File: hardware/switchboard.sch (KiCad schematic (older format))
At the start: 0 parts

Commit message: hardware: add terminal blocks
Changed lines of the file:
@@
 $Descr A4 11693 8268
 encoding utf-8
-Sheet 1 3
+Sheet 1 4
 Title ""
 Date ""
@@
 $EndDescr
 $Sheet
-S 3085 2165 1515 1345
+S 3085 2165 1625 3010
 U 605C1303
 F0 "Relays" 50
 F1 "relays.sch" 50
+F2 "DOME_LIGHTS" I R 4710 2320 50
+F3 "WATER_PUMP" I R 4710 2450 50
+F4 "FRIDGE" I R 4710 2575 50
+F5 "STRIP_LIGHTS" I R 4710 2695 50
+F6 "REAR_FLOOD" I R 4710 2815 50
+F7 "DRIVER_FLOOD" I R 4710 2900 50
+F8 "PASS_FLOOD" I R 4710 3035 50
+F9 "DIESEL_HEATER" I R 4710 3160 50
+F10 "DOME_LIGHTS_CTRL" I L 3085 2535 50
+F11 "WATER_PUMP_CTRL" I L 3085 2355 50
+F12 "FRIDGE_CTRL" I L 3085 2630 50
+F13 "STRIP_LIGHTS_CTRL" I L 3085 2750 50
+F14 "DIESEL_HEATER_CTRL" I L 3085 2905 50
+F15 "PASS_FLOOD_CTRL" I L 3085 3075 50
+F16 "DRIVER_FLOOD_CTRL" I L 3085 3245 50
+F17 "REAR_FLOOD_CTRL" I L 3085 3400 50
+F18 "SHOWER_FAN" I R 4710 3350 50
+F19 "SHOWER_FAN_CTRL" I L 3085 3555 50
+F20 "KITCHEN_FAN" I R 4710 3530 50
+F21 "KITCHEN_FAN_CTRL" I L 3085 3720 50
+F22 "BAR_LIGHT" I R 4710 3700 50
+F23 "BAR_LIGHT_CTRL" I L 3085 3890 50
+F24 "COMP_1_LIGHT_CTRL" I L 3085 4045 50
+F25 "COMP_1_LIGHT" I R 4710 3840 50
+F26 "COMP_4_LIGHT" I R 4710 3975 50
+F27 "COMP_4_LIGHT_CTRL" I L 3085 4190 50
+F28 "COMP_3_LIGHT" I R 4710 4110 50
+F29 "COMP_3_LIGHT_CTRL" I L 3085 4310 50
+F30 "COMP_2_LIGHT" I R 4710 4270 50
+F31 "COMP_2_LIGHT_CTRL" I L 3085 4410 50
+F32 "COMP_5_LIGHT_CTRL" I L 3085 4510 50
+F33 "COMP_5_LIGHT" I R 4710 4385 50
+F34 "AUX_RLY_1" I R 4710 4500 50
+F35 "AUX_RLY_1_CTRL" I L 3085 4695 50
+F36 "AUX_RLY_2" I R 4710 4635 50
+F37 "AUX_RLY_2_CTRL" I L 3085 4800 50
+F38 "AUX_RLY_3" I R 4710 4765 50
+F39 "AUX_RLY_3_CTRL" I L 3085 4905 50
+F40 "AUX_RLY_4" I R 4710 4880 50
+F41 "AUX_RLY_4_CTRL" I L 3085 5000 50
 $EndSheet
 $Sheet
@@
 F0 "Connectors" 50
 F1 "connectors.sch" 50
-F2 "P1[1..12]" I L 5825 2105 50
-F3 "P2[1..12]" I L 5825 2220 50
-F4 "P3[1..12]" I L 5825 2340 50
-F5 "P4[1..12]" I L 5825 2455 50
-F6 "P5[1..12]" I L 5825 2570 50
-F7 "P6[1..12]" I L 5825 2690 50
-F8 "P7[1..12]" I L 5825 2820 50
-F9 "P8[1..12]" I L 5825 2950 50
-F10 "P9[1..12]" I L 5825 3070 50
-F11 "P10[1..12]" I L 5825 3190 50
-F12 "P11[1..12]" I L 5825 3310 50
-F13 "P12[1..12]" I L 5825 3430 50
-F14 "AUX_SW_1" I R 7000 2180 50
-F15 "AUX_SW_2" I R 7000 2310 50
-F16 "AUX_SW_3" I R 7000 2425 50
-F17 "AUX_SW_4" I R 7000 2535 50
+$EndSheet
+$Sheet
+S 7625 4050 1090 1145
+U 60B2977E
+F0 "Terminal Blocks" 50
+F1 "terminal_blocks.sch" 50
+F2 "AUX_SW_1" I R 8715 4245 50
+F3 "AUX_SW_2" I R 8715 4355 50
+F4 "AUX_SW_3" I R 8715 4475 50
+F5 "AUX_SW_4" I R 8715 4595 50
 $EndSheet
 $EndSCHEMATC

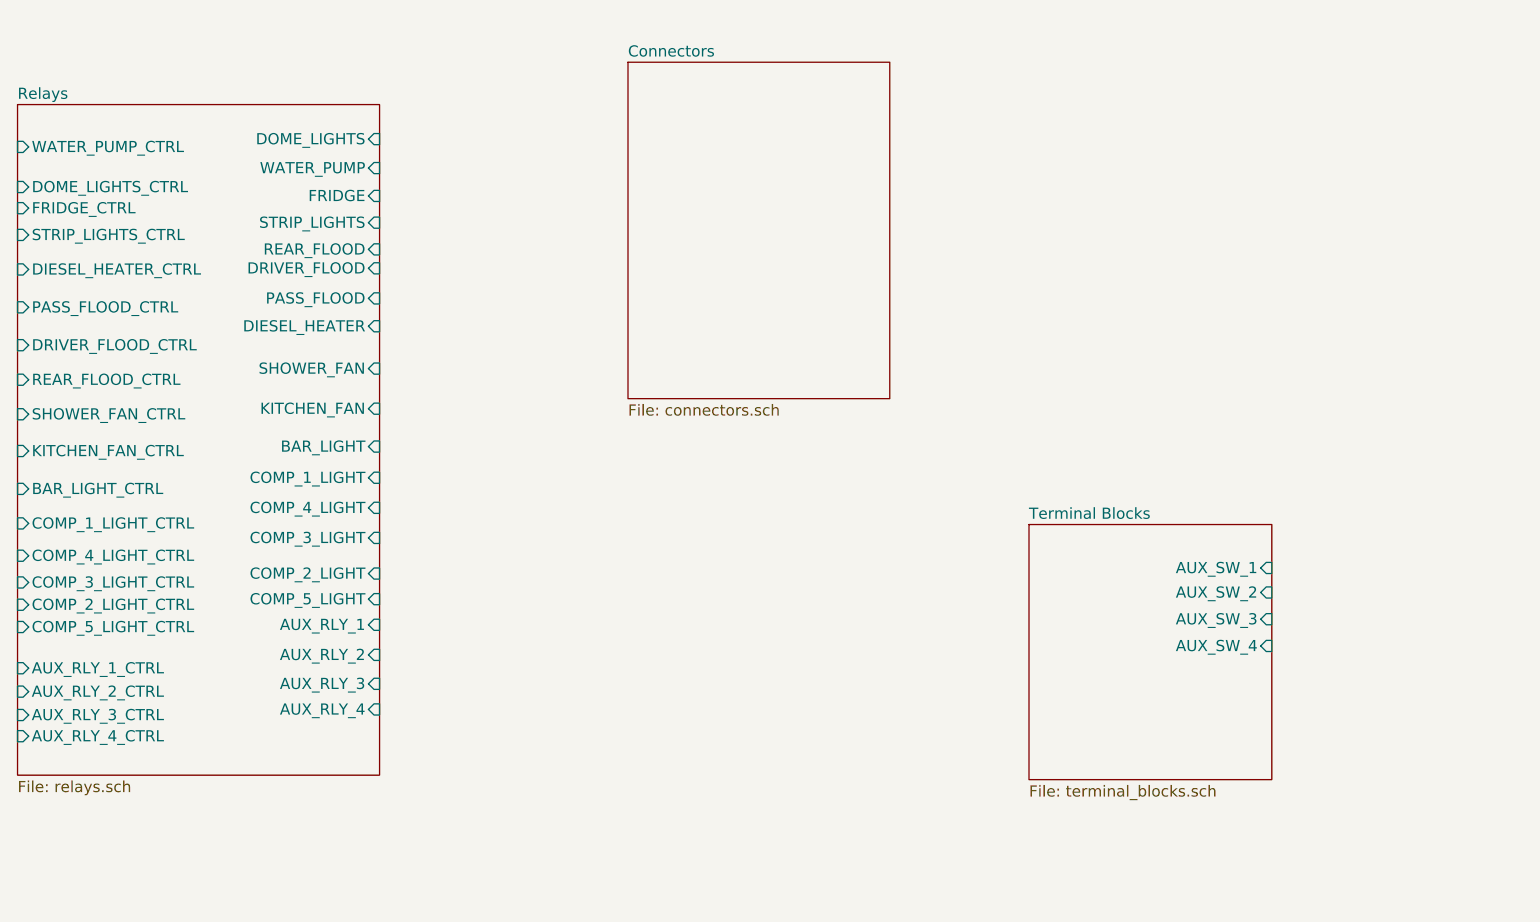
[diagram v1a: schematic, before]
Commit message: hardware: adjust relay hierarchical pins
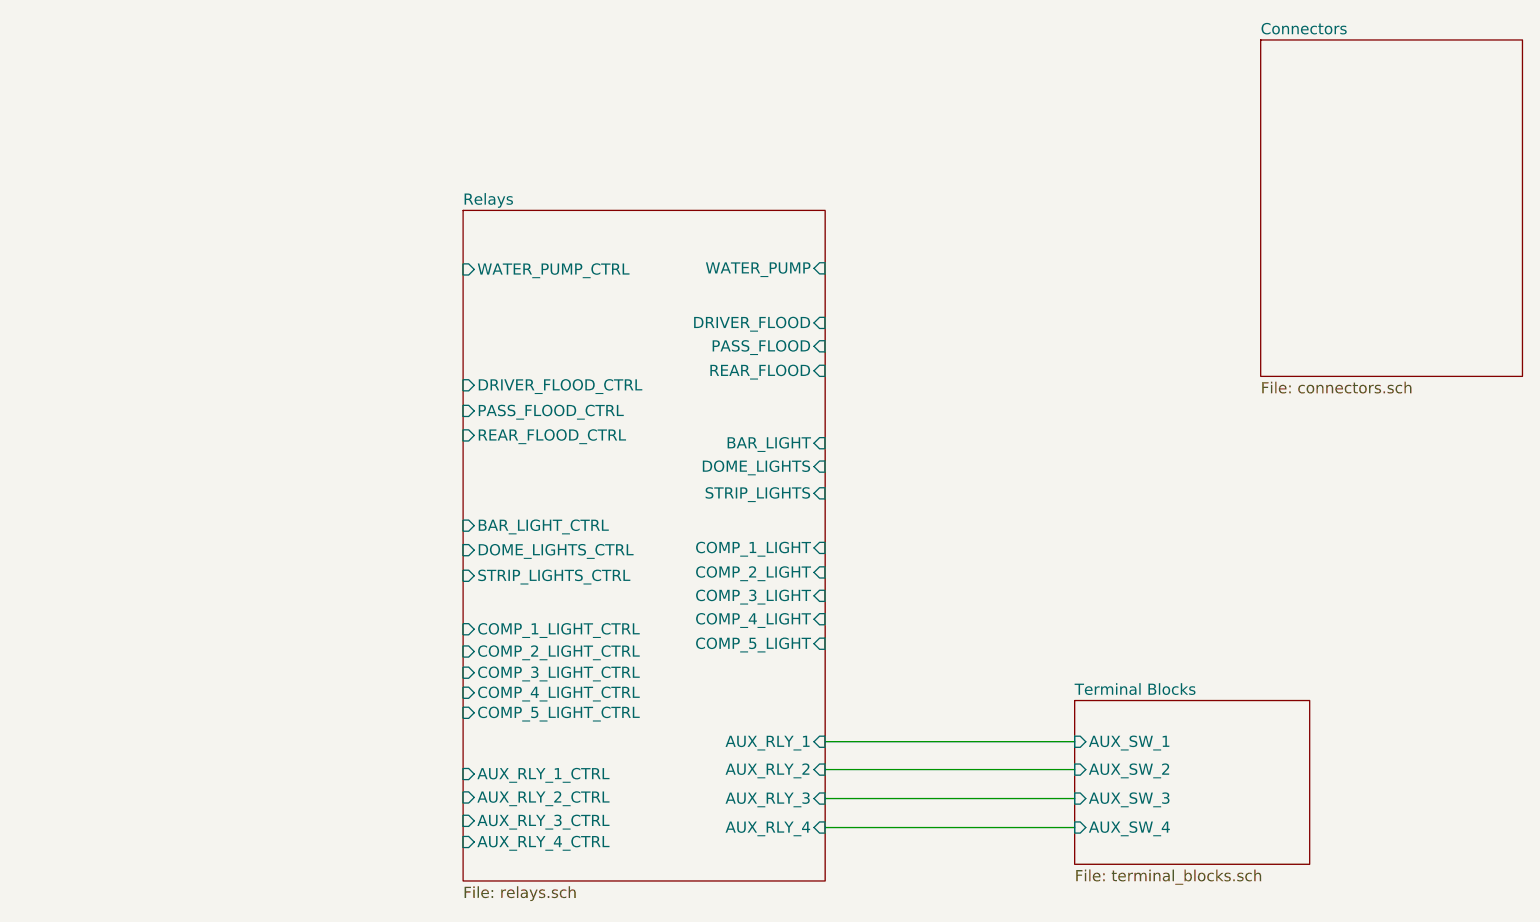
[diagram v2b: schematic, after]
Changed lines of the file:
@@
 $Descr A4 11693 8268
 encoding utf-8
-Sheet 1 4
+Sheet 1 5
 Title ""
 Date ""
@@
 $EndDescr
 $Sheet
-S 3085 2165 1625 3010
+S 5085 2640 1625 3010
 U 605C1303
 F0 "Relays" 50
 F1 "relays.sch" 50
-F2 "DOME_LIGHTS" I R 4710 2320 50
-F3 "WATER_PUMP" I R 4710 2450 50
-F4 "FRIDGE" I R 4710 2575 50
-F5 "STRIP_LIGHTS" I R 4710 2695 50
-F6 "REAR_FLOOD" I R 4710 2815 50
-F7 "DRIVER_FLOOD" I R 4710 2900 50
-F8 "PASS_FLOOD" I R 4710 3035 50
-F9 "DIESEL_HEATER" I R 4710 3160 50
-F10 "DOME_LIGHTS_CTRL" I L 3085 2535 50
-F11 "WATER_PUMP_CTRL" I L 3085 2355 50
-F12 "FRIDGE_CTRL" I L 3085 2630 50
-F13 "STRIP_LIGHTS_CTRL" I L 3085 2750 50
-F14 "DIESEL_HEATER_CTRL" I L 3085 2905 50
-F15 "PASS_FLOOD_CTRL" I L 3085 3075 50
-F16 "DRIVER_FLOOD_CTRL" I L 3085 3245 50
-F17 "REAR_FLOOD_CTRL" I L 3085 3400 50
-F18 "SHOWER_FAN" I R 4710 3350 50
-F19 "SHOWER_FAN_CTRL" I L 3085 3555 50
-F20 "KITCHEN_FAN" I R 4710 3530 50
-F21 "KITCHEN_FAN_CTRL" I L 3085 3720 50
-F22 "BAR_LIGHT" I R 4710 3700 50
-F23 "BAR_LIGHT_CTRL" I L 3085 3890 50
-F24 "COMP_1_LIGHT_CTRL" I L 3085 4045 50
-F25 "COMP_1_LIGHT" I R 4710 3840 50
-F26 "COMP_4_LIGHT" I R 4710 3975 50
-F27 "COMP_4_LIGHT_CTRL" I L 3085 4190 50
-F28 "COMP_3_LIGHT" I R 4710 4110 50
-F29 "COMP_3_LIGHT_CTRL" I L 3085 4310 50
-F30 "COMP_2_LIGHT" I R 4710 4270 50
-F31 "COMP_2_LIGHT_CTRL" I L 3085 4410 50
-F32 "COMP_5_LIGHT_CTRL" I L 3085 4510 50
-F33 "COMP_5_LIGHT" I R 4710 4385 50
-F34 "AUX_RLY_1" I R 4710 4500 50
-F35 "AUX_RLY_1_CTRL" I L 3085 4695 50
-F36 "AUX_RLY_2" I R 4710 4635 50
-F37 "AUX_RLY_2_CTRL" I L 3085 4800 50
-F38 "AUX_RLY_3" I R 4710 4765 50
-F39 "AUX_RLY_3_CTRL" I L 3085 4905 50
-F40 "AUX_RLY_4" I R 4710 4880 50
-F41 "AUX_RLY_4_CTRL" I L 3085 5000 50
+F2 "DOME_LIGHTS" I R 6710 3790 50
+F3 "WATER_PUMP" I R 6710 2900 50
+F4 "STRIP_LIGHTS" I R 6710 3910 50
+F5 "REAR_FLOOD" I R 6710 3360 50
+F6 "DRIVER_FLOOD" I R 6710 3145 50
+F7 "PASS_FLOOD" I R 6710 3250 50
+F8 "DOME_LIGHTS_CTRL" I L 5085 4165 50
+F9 "WATER_PUMP_CTRL" I L 5085 2905 50
+F10 "STRIP_LIGHTS_CTRL" I L 5085 4280 50
+F11 "PASS_FLOOD_CTRL" I L 5085 3540 50
+F12 "DRIVER_FLOOD_CTRL" I L 5085 3425 50
+F13 "REAR_FLOOD_CTRL" I L 5085 3650 50
+F14 "BAR_LIGHT" I R 6710 3685 50
+F15 "BAR_LIGHT_CTRL" I L 5085 4055 50
+F16 "COMP_1_LIGHT_CTRL" I L 5085 4520 50
+F17 "COMP_1_LIGHT" I R 6710 4155 50
+F18 "COMP_4_LIGHT" I R 6710 4475 50
+F19 "COMP_4_LIGHT_CTRL" I L 5085 4805 50
+F20 "COMP_3_LIGHT" I R 6710 4370 50
+F21 "COMP_3_LIGHT_CTRL" I L 5085 4715 50
+F22 "COMP_2_LIGHT" I R 6710 4265 50
+F23 "COMP_2_LIGHT_CTRL" I L 5085 4620 50
+F24 "COMP_5_LIGHT_CTRL" I L 5085 4895 50
+F25 "COMP_5_LIGHT" I R 6710 4585 50
+F26 "AUX_RLY_1" I R 6710 5025 50
+F27 "AUX_RLY_1_CTRL" I L 5085 5170 50
+F28 "AUX_RLY_2" I R 6710 5150 50
+F29 "AUX_RLY_2_CTRL" I L 5085 5275 50
+F30 "AUX_RLY_3" I R 6710 5280 50
+F31 "AUX_RLY_3_CTRL" I L 5085 5380 50
+F32 "AUX_RLY_4" I R 6710 5410 50
+F33 "AUX_RLY_4_CTRL" I L 5085 5475 50
 $EndSheet
 $Sheet
-S 5825 1975 1175 1510
+S 8665 1875 1175 1510
 U 605C149A
 F0 "Connectors" 50
@@
 $EndSheet
 $Sheet
-S 7625 4050 1090 1145
+S 7830 4840 1055 735
 U 60B2977E
 F0 "Terminal Blocks" 50
 F1 "terminal_blocks.sch" 50
-F2 "AUX_SW_1" I R 8715 4245 50
-F3 "AUX_SW_2" I R 8715 4355 50
-F4 "AUX_SW_3" I R 8715 4475 50
-F5 "AUX_SW_4" I R 8715 4595 50
+F2 "AUX_SW_1" I L 7830 5025 50
+F3 "AUX_SW_2" I L 7830 5150 50
+F4 "AUX_SW_3" I L 7830 5280 50
+F5 "AUX_SW_4" I L 7830 5410 50
 $EndSheet
+Wire Wire Line
+	6710 5025 7830 5025
+Wire Wire Line
+	6710 5150 7830 5150
+Wire Wire Line
+	6710 5280 7830 5280
+Wire Wire Line
+	6710 5410 7830 5410
 $EndSCHEMATC
